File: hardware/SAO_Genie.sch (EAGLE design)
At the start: 24 parts, among them J1 CONN_02X2_NO_SILK, J2 SAO OUT, U4 ATSAMD21G-A, Y1 32.768KHZ

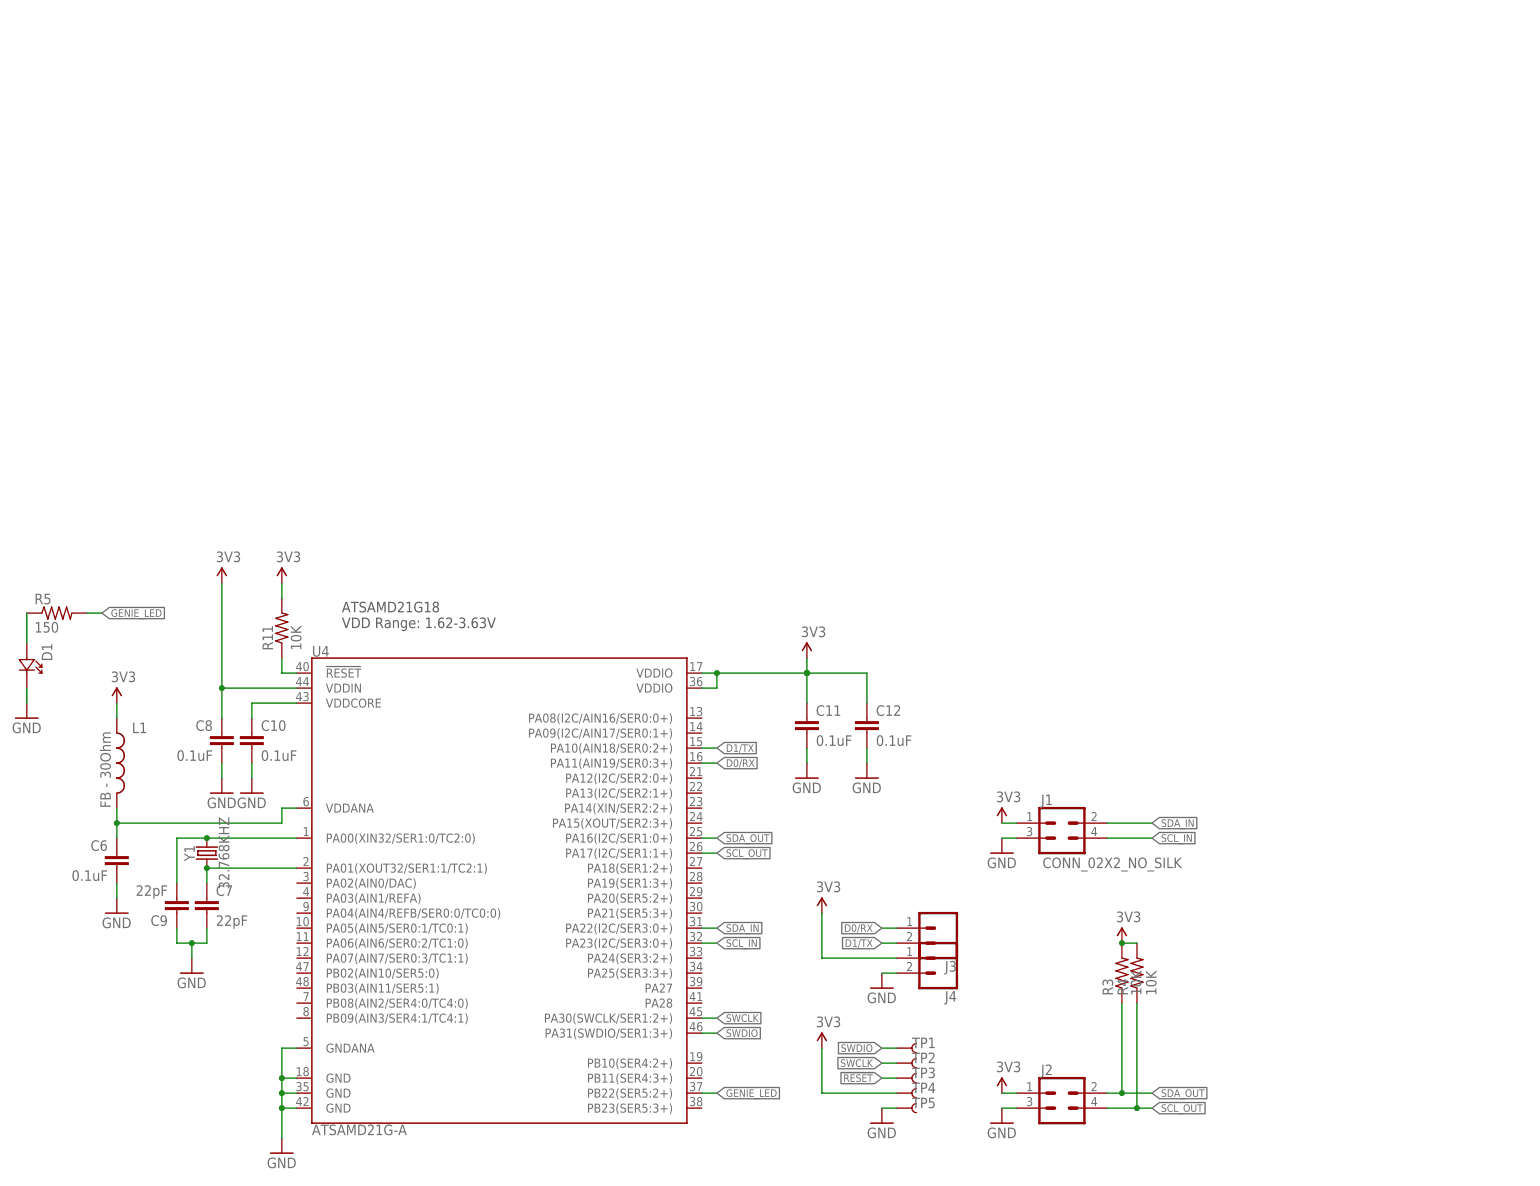
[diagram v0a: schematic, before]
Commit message: update hardware schematic, board layout, and bill of material
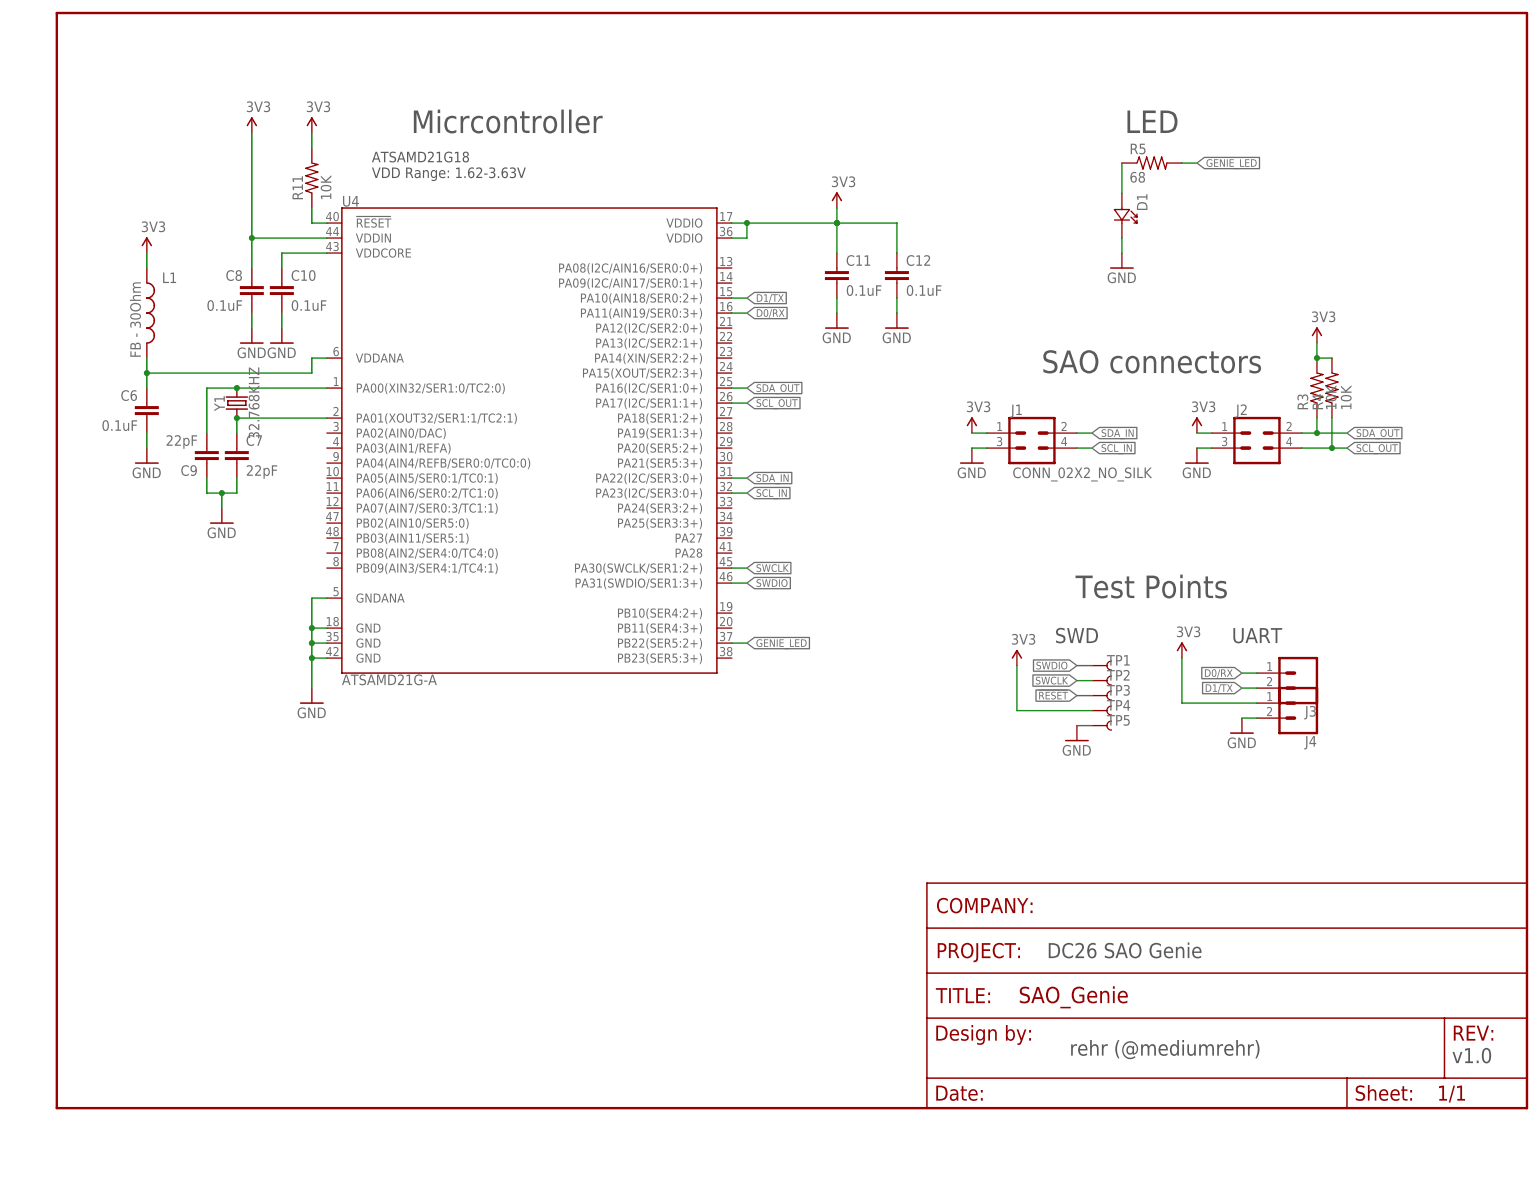
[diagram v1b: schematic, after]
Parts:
- added FRAME1: FRAME-LETTER-BLANKNO_PACKAGE, SparkFun-Aesthetics:FRAME-LETTER-BLANKNO_PACKAGE
- R5: value 150 -> 68
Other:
- note added: "DC26 SAO Genie"
- note added: "LED"
- note added: "Micrcontroller"
- note added: "SAO connectors"
- note added: "SWD"
- note added: "Test Points"
- note added: "UART"
- note added: "rehr (@mediumrehr)"
- note added: "v1.0"
- moved on the sheet: C10, C11, C12, C6, C7, C8, C9, D1, J1, J2, J3, J4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
